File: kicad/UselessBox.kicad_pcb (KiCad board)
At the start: 2 copper layers, 46.5 x 36 mm, 21 parts, among them J1 Screw_Terminal_01x02, J2 Screw_Terminal_01x02, J4 Servo, Q1 IRF9540N, Q2 BC548, SW1 DPDT, U1 NE555P, U2 NE555P

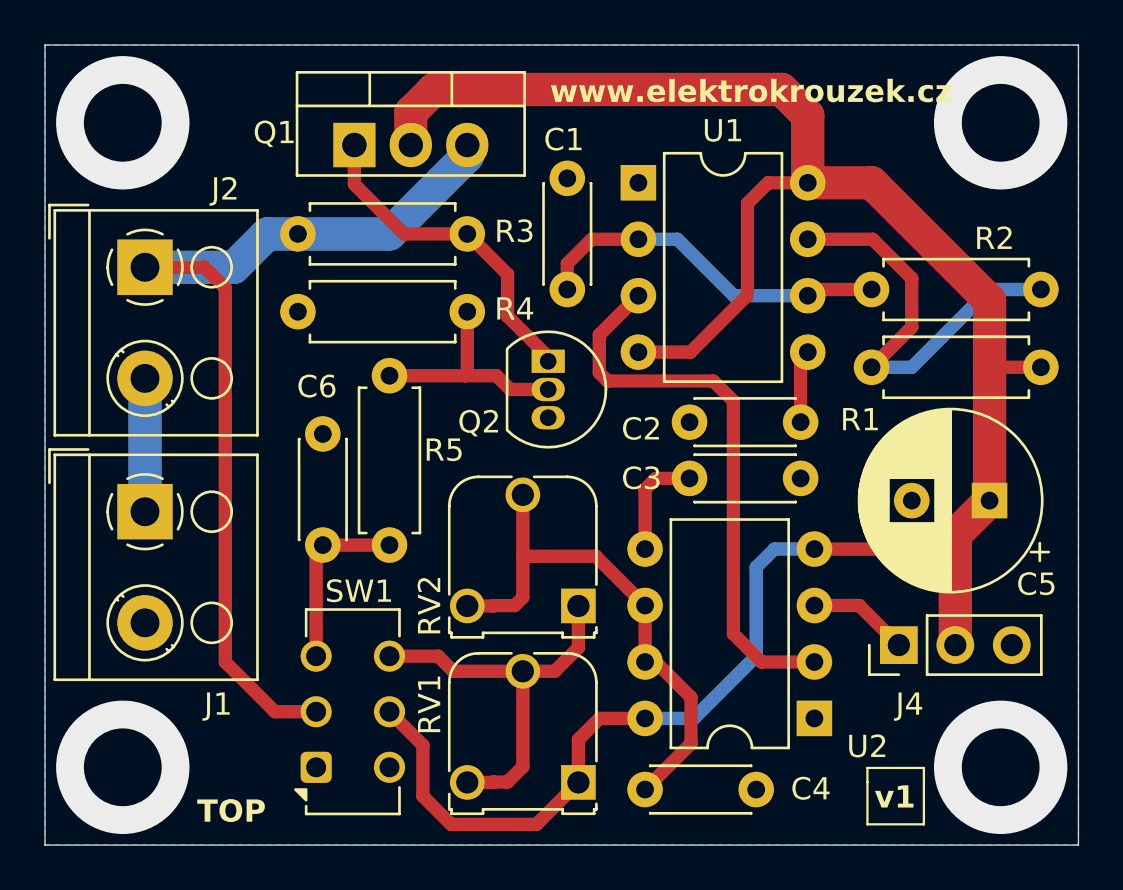
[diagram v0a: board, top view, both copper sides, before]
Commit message: Turn-on jumper added
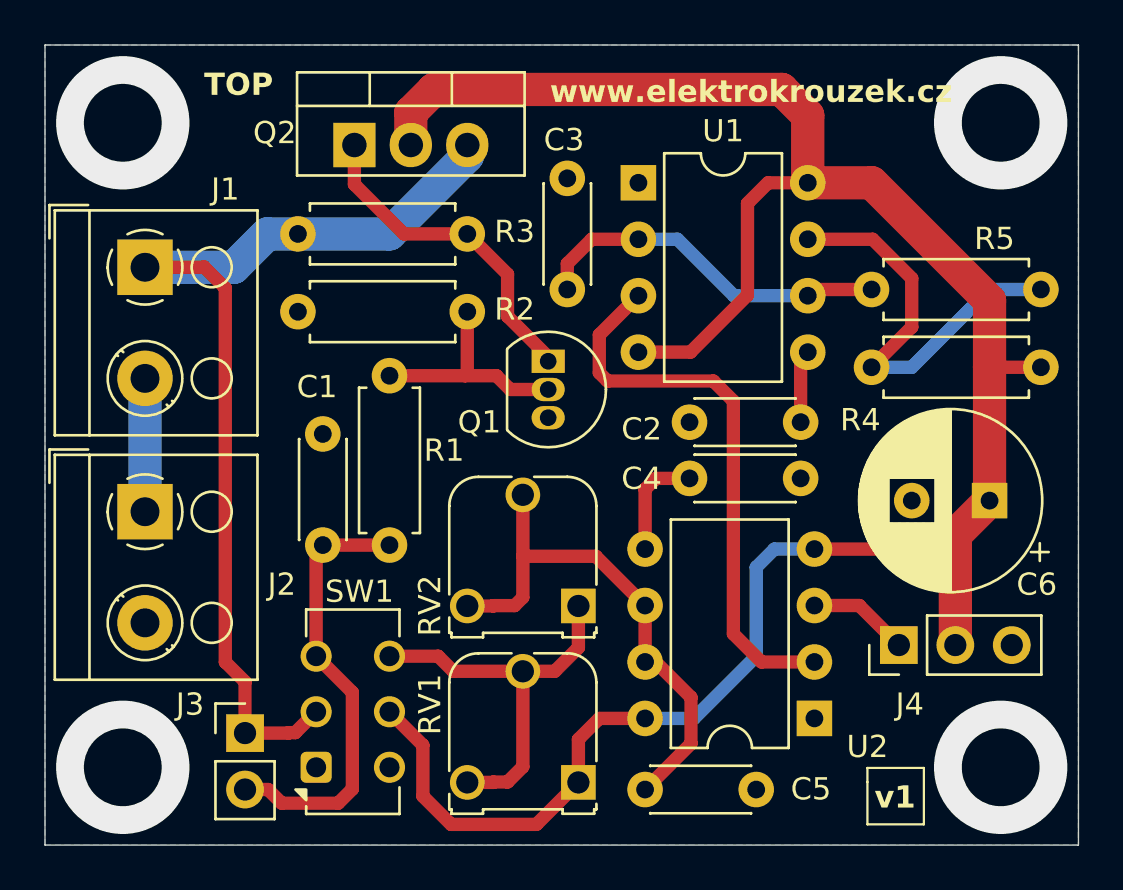
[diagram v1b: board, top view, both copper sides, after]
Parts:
- added J3: Turn on jumper, Connector_PinHeader_2.54mm:PinHeader_1x02_P2.54mm_Vertical, F.Cu at (139.0, 91.5)
- renumbered C6 to C1, C1 to C3, C3 to C4, C4 to C5, C5 to C6, J2 to J1, J1 to J2, Q2 to Q1, Q1 to Q2, R5 to R1, R4 to R2, R1 to R4, R2 to R5
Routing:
- net ON: track 8.12 -> 20.1 mm
- net +6V: track 42.9 -> 45.1 mm
